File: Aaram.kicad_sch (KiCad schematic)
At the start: 51 parts, among them J1 Conn_01x03, J2 Conn_01x02, J3 AC_OUT, J4 SWITCH_IN, J5 5V_OUT, J6 PSU_AC_IN, J8 SPARE_PINS, K1 10A cube relay, K2 10A cube relay, K3 10A cube relay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

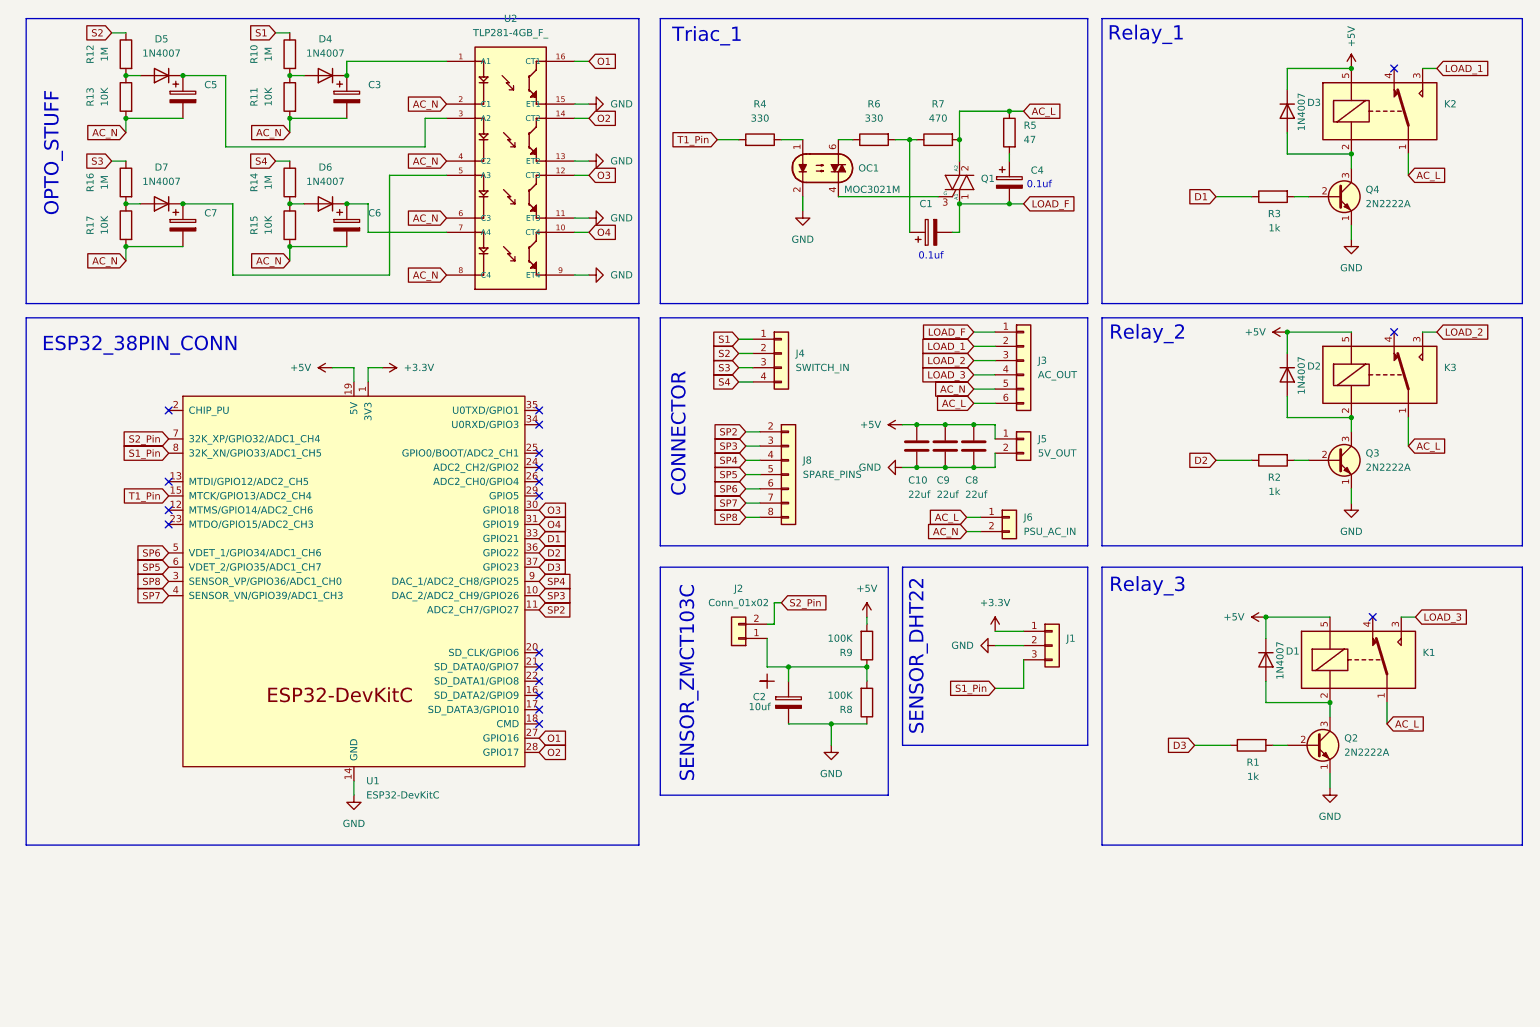
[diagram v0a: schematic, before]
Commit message: Major Update
1. Added MOVs for high voltage protection
2. Added support for zero cross detection
3. Used SMD components where possible
4. Better AC detection
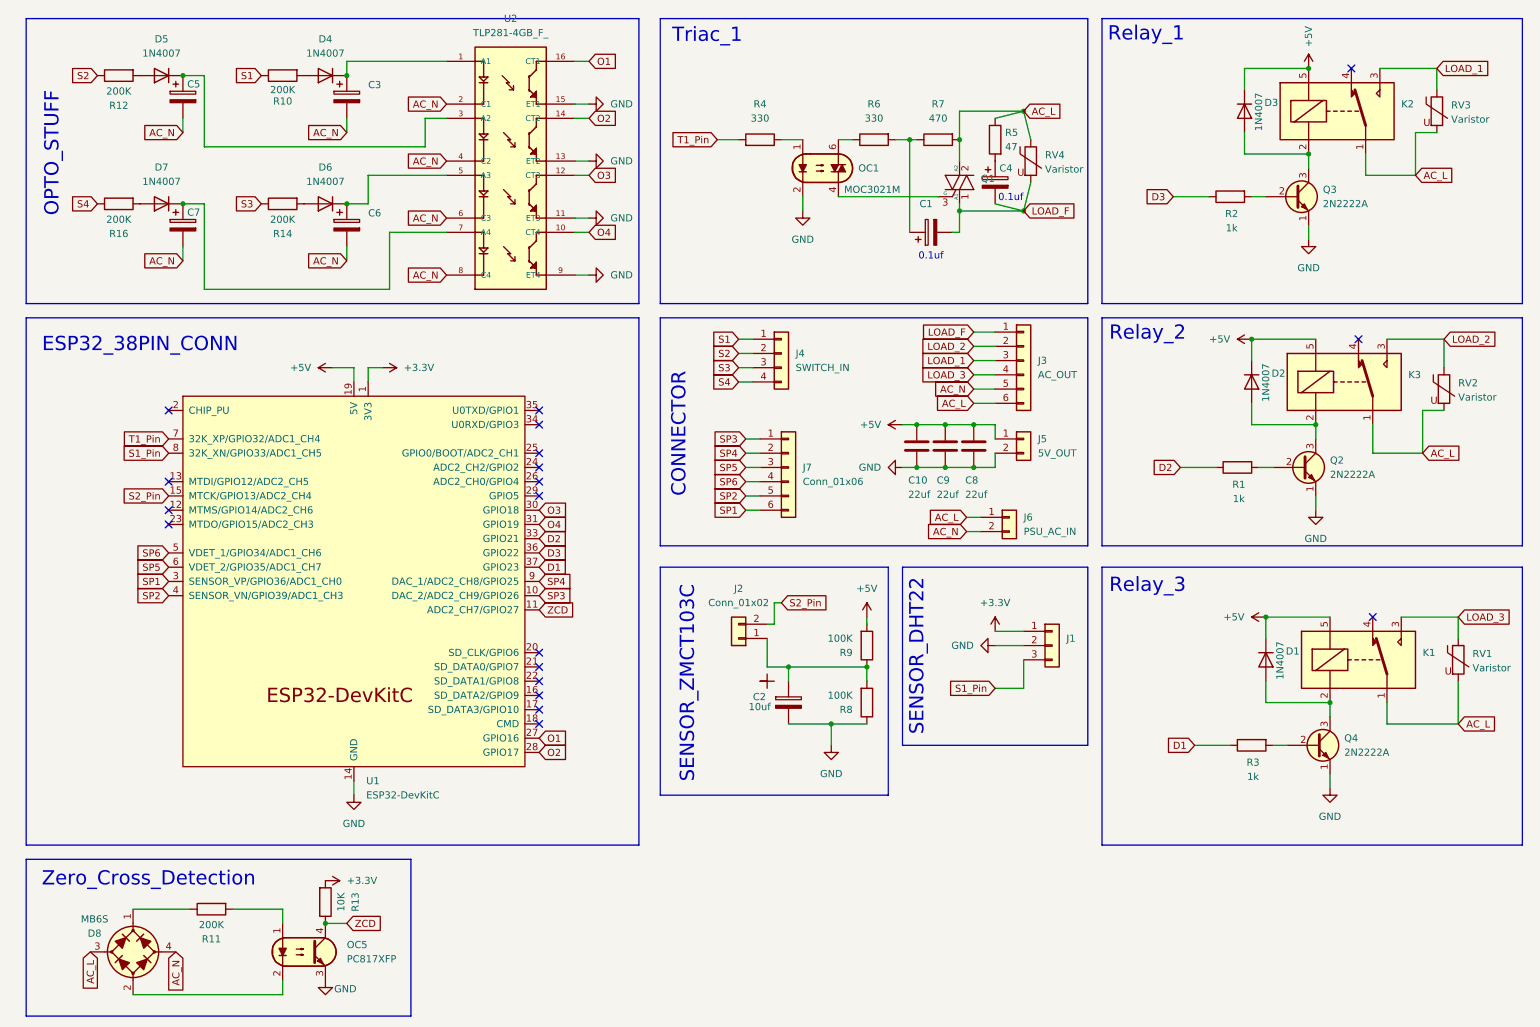
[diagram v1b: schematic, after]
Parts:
- removed J8: SPARE_PINS, Connector_PinHeader_2.54mm:PinHeader_1x08_P2.54mm_Vertical, symbol Connector_Generic:Conn_01x08
- removed R15, R17: 10K, PCM_Capacitor_SMD_Handsoldering_AKL:C_1206_3216Metric_Pad1.42x1.75mm, symbol PCM_Resistor_AKL:R_1206
- added D8: MB6S, PCM_Diode_SMD_AKL:Diode_Bridge_MBS, symbol PCM_Diode_Bridge_AKL:MB6S
- added J7: Conn_01x06, Connector_PinHeader_2.54mm:PinHeader_1x06_P2.54mm_Vertical, symbol Connector_Generic:Conn_01x06
- added OC5: PC817XFP, PCM_Package_DIP_AKL:SMDIP-4_W11.48mm, symbol PCM_Optocoupler_AKL:PC817XFP
- added RV1, RV2, RV3, RV4: Varistor, Xicor_Custom stuff:Varistor_10D431K, symbol Device:Varistor
- R10, R12, R14, R16: value 1M -> 200K
- R11: value 10K -> 200K
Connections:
- net SP7 is gone; now on net SP2: U1.4 (SENSOR_VN/GPIO39/ADC1_CH3)
- net +3.3V: now also R13.1
- net AC_L: now also D8.3 (1), RV1.2, RV2.2, RV3.2, RV4.1
- net AC_N: now also D8.4 (2); no longer R11.1, R13.1
- net D1: now also U1.37 (GPIO23); no longer U1.33 (GPIO21)
- net D2: now also R1.2, U1.33 (GPIO21); no longer R2.2, U1.36 (GPIO22)
- net D3: now also R2.2, U1.36 (GPIO22); no longer R1.2, U1.37 (GPIO23)
- net GND: now also OC5.3
- net LOAD_1: now also J3.3 (Pin_3), RV3.1; no longer J3.2 (Pin_2)
- net LOAD_2: now also J3.2 (Pin_2), RV2.1; no longer J3.3 (Pin_3)
- net LOAD_3: now also RV1.1
- net LOAD_F: now also RV4.2
- net S2_Pin: now also U1.15 (MTCK/GPIO13/ADC2_CH4); no longer U1.7 (32K_XP/GPIO32/ADC1_CH4)
- net S3: now also R14.2; no longer R16.2
- net S4: now also R16.2; no longer R14.2
- net SP2: now also J7.5 (Pin_5); no longer U1.11 (ADC2_CH7/GPIO27)
- net SP3: now also J7.1 (Pin_1)
- net SP4: now also J7.2 (Pin_2)
- net SP5: now also J7.3 (Pin_3)
- net SP6: now also J7.4 (Pin_4)
- net T1_Pin: now also U1.7 (32K_XP/GPIO32/ADC1_CH4); no longer U1.15 (MTCK/GPIO13/ADC2_CH4)
- net at D2.2 (A), K3.2: now also Q2.3 (C); no longer Q3.3 (C)
- net at D4.2 (A), R10.1: no longer R11.2
- net at D5.2 (A), R12.1: no longer R13.2
- net at D3.2 (A), K2.2: now also Q3.3 (C); no longer Q4.3 (C)
- net at C6.1, D6.1 (K): now also U2.5 (A3); no longer U2.7 (A4)
- net at C7.1, D7.1 (K): now also U2.7 (A4); no longer U2.5 (A3)
- net at D1.2 (A), K1.2: now also Q4.3 (C); no longer Q2.3 (C)
- net SP8 renamed SP1
- net SP1: now also J7.6 (Pin_6)
- new net: D8.1 (+), R11.2
- new net: D8.2 (-), OC5.2
- new net: OC5.1, R11.1
- new net ZCD: OC5.4, R13.2, U1.11 (ADC2_CH7/GPIO27)
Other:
- note added: "Zero_Cross_Detection"
- moved on the sheet: C4, D2, D3, K2, K3, R10, R12, R14, R16, R5

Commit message: Change footprinnt
Changed transistor footprint
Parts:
- Q2, Q3, Q4: footprint PCM_Package_TO_SOT_SMD_AKL:SOT-23_BigPads -> PCM_Package_TO_SOT_THT_AKL:TO-18-3_EBC
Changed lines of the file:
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@@
 			)
 		)
-		(property "Footprint" "PCM_Package_TO_SOT_SMD_AKL:SOT-23_BigPads"
+		(property "Footprint" "PCM_Package_TO_SOT_THT_AKL:TO-18-3_EBC"
 			(at 247.65 92.71 0)
 			(effects
@@
 			)
 		)
-		(property "Footprint" "PCM_Package_TO_SOT_SMD_AKL:SOT-23_BigPads"
+		(property "Footprint" "PCM_Package_TO_SOT_THT_AKL:TO-18-3_EBC"
 			(at 246.38 44.45 0)
 			(effects
@@
 			)
 		)
-		(property "Footprint" "PCM_Package_TO_SOT_SMD_AKL:SOT-23_BigPads"
+		(property "Footprint" "PCM_Package_TO_SOT_THT_AKL:TO-18-3_EBC"
 			(at 250.19 142.24 0)
 			(effects
